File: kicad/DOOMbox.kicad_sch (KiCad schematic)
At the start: 13 parts, among them J1 DE15_Socket_HighDensity, U1 RPi Pico 2, U2 MCP23S08

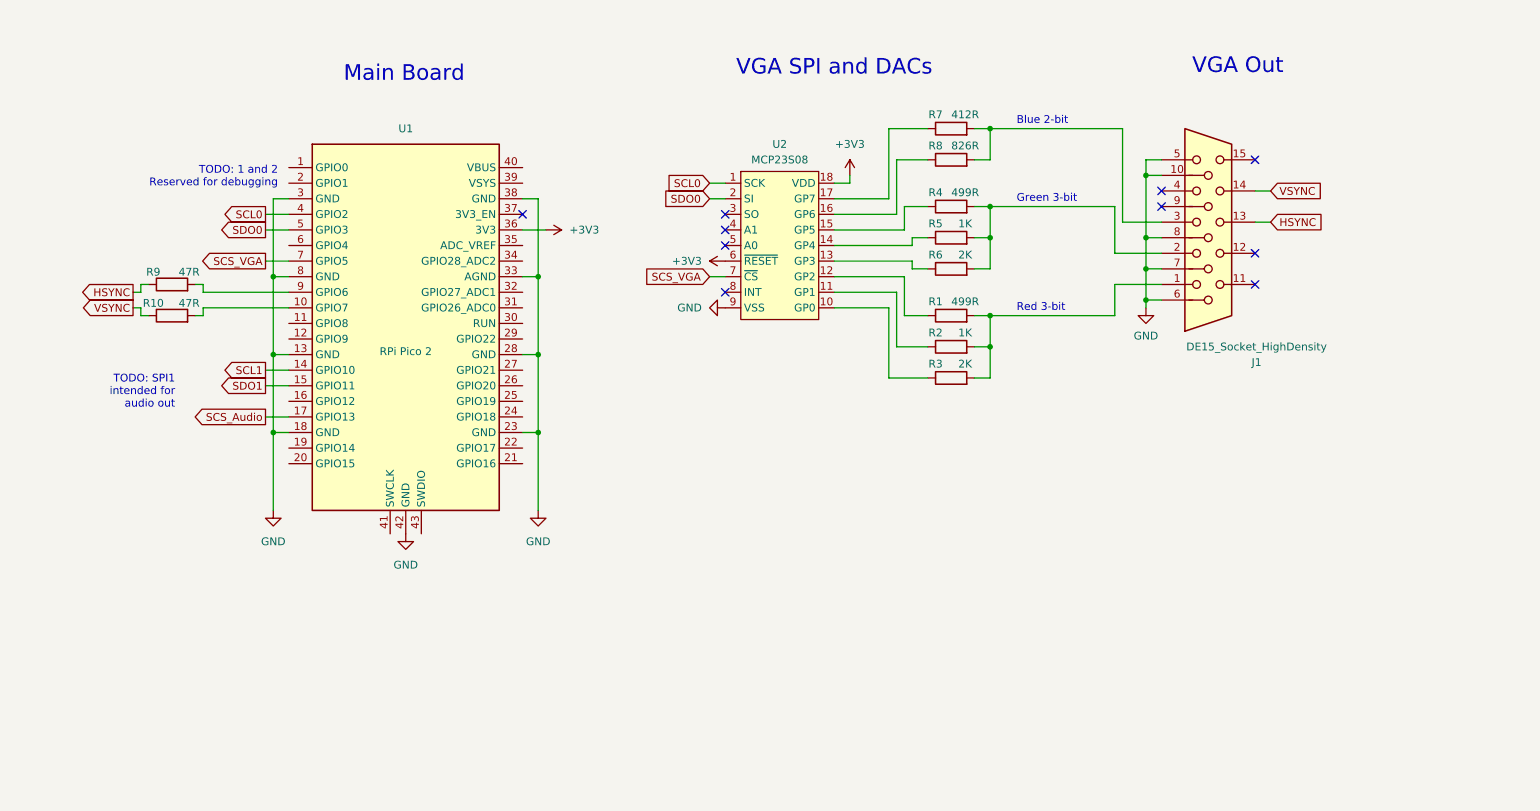
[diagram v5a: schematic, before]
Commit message: Document inputs and storage info, and add PWM audio schematic
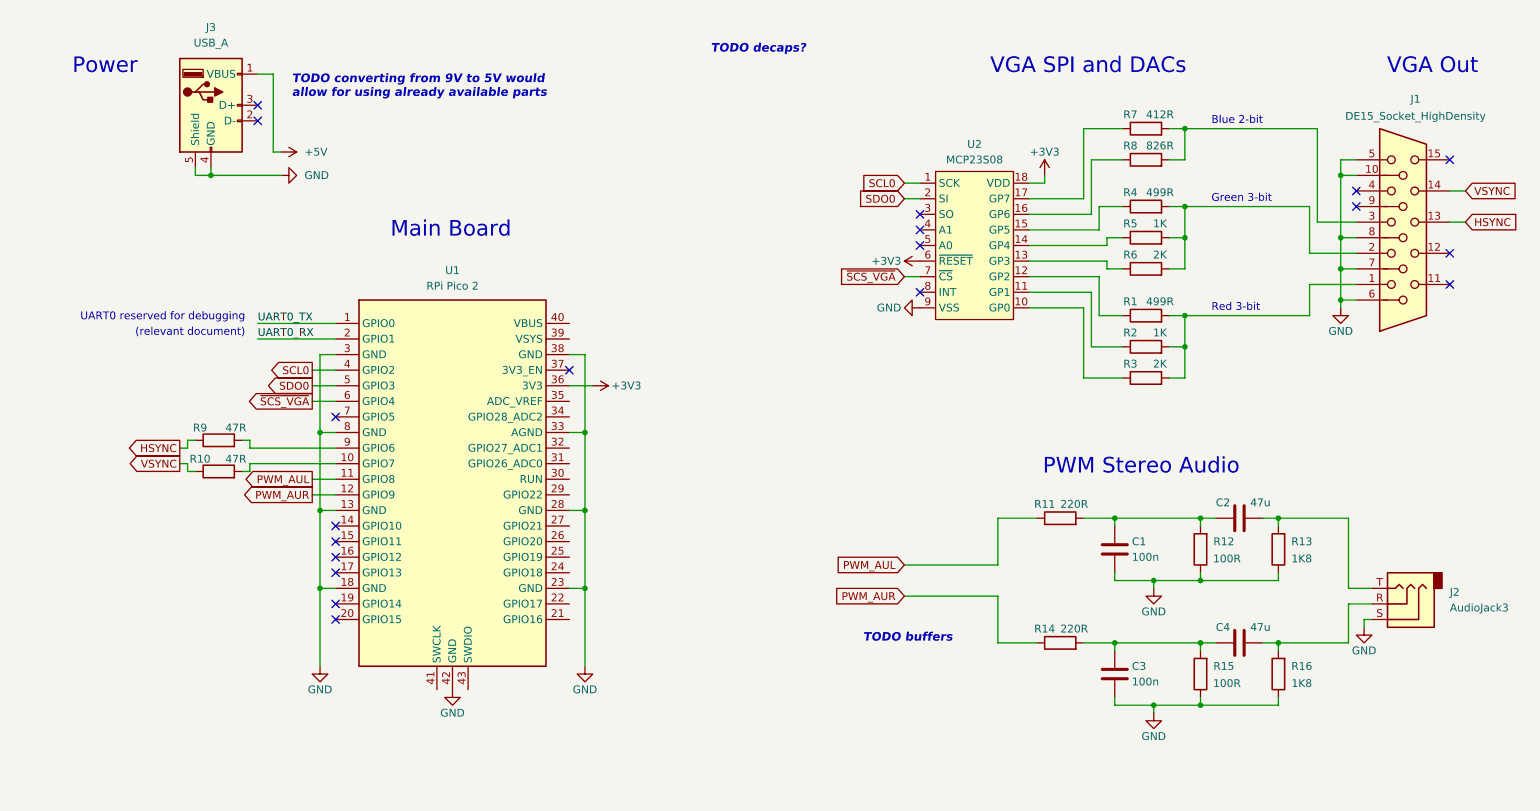
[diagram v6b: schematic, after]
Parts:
- added C1, C3: 100n, symbol Device:C
- added C2, C4: 47u, symbol Device:C
- added J2: AudioJack3, symbol Connector_Audio:AudioJack3
- added J3: USB_A, symbol Connector:USB_A
- added R11, R14: 220R, symbol Device:R
- added R12, R15: 100R, symbol Device:R
- added R13, R16: 1K8, symbol Device:R
- U1: symbol MCU_RPi:RPi_Pico_SMD_TH -> Doombox:RPi_Pico_SMD_TH
- U2: symbol MCU_Microchip_MCP:MCP23S08 -> Doombox:MCP23S08
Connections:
- net GND: now also C1.2, C3.2, J2.S, J3.4 (GND), J3.5 (Shield), R12.1, R13.1, R15.1, R16.1
- net UART0_TX: now reaches U1.1 (GPIO0)
- net PWM_AUL: now reaches U1.11 (GPIO8)
- net PWM_AUL: now also R11.1
- net PWM_AUR: now reaches U1.12 (GPIO9)
- net PWM_AUR: now also R14.1
- net UART0_RX: now reaches U1.2 (GPIO1)
- net ~{SCS_VGA}: now reaches U1.6 (GPIO4)
- net ~{SCS_VGA}: now also U2.7 (~{CS})
- net SCL1: no longer names the net of U1.14 (GPIO10)
- net SCS_Audio: no longer names the net of U1.17 (GPIO13)
- net SCS_VGA: no longer names the net of U1.7 (GPIO5)
- net SCS_VGA: no longer U2.7 (~{CS})
- net SDO1: no longer names the net of U1.15 (GPIO11)
- new net: C2.2, J2.T, R13.2
- new net: C3.1, C4.1, R14.2, R15.2
- new net: C1.1, C2.1, R11.2, R12.2
- new net: C4.2, J2.R, R16.2
- new net +5V: J3.1 (VBUS)
- no-connect marks 10 -> 19
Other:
- note added: "(relevant document)"
- note added: "PWM Stereo Audio"
- note added: "Power"
- note added: "TODO buffers"
- note added: "TODO converting from 9V to 5V would allow for using already available parts"
- note added: "TODO decaps?"
- note added: "UART0 reserved for debugging"
- note removed: "TODO: 1 and 2 Reserved for debugging"
- note removed: "TODO: SPI1 intended for audio out"
- company: (none) -> Jack Bennett
- title: (none) -> The DOOMbox
- moved on the sheet: J1, R1, R10, R2, R3, R4, R5, R6, R7, R8, R9, U1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

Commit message: Schem for power circuit + rpi SWD pins and reset button
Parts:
- removed J3: USB_A, symbol Connector:USB_A
- added C5: 1u, symbol Device:C
- added C6: 2u2, symbol Device:C
- added D1: D, symbol Device:D
- added D2: LED, symbol Device:LED
- added R17: 220R, symbol Device:R
- added SW1: SW_SPST, symbol Switch:SW_SPST
- added SW2: SW_Push, symbol Switch:SW_Push
- added U3: AP7381-50SA-7, Package_TO_SOT_SMD:SOT-23, symbol Regulator_Linear:AP7381-50SA-7
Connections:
- net +5V: now also C6.1, D1.2 (A), D2.1 (K), R17.1, U3.2 (VO)
- net GND: now also C5.2, C6.2, SW2.2, U3.3 (GND)
- net at U1.30 (RUN): now also SW2.1
- net at U1.39 (VSYS): now also D1.1 (K)
- net SWCLK: now reaches U1.41 (SWCLK)
- net SWDIO: now reaches U1.43 (SWDIO)
- new net: C5.1, SW1.2 (B), U3.1 (VI)
- new net: D2.2 (A), R17.2
- new net VDC: SW1.1 (A)
- no-connect marks 19 -> 11
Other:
- note added: "To order (not yet doc'd): - necessary resistors - necessary caps - diodes? (if schottky needed) - phone connector (J2)"
- note added: "UART0 reserved for debugging (so is SWD, also for programming)"
- note added: "power LED worth ~20mA?"
- note removed: "(relevant document)"
- note removed: "TODO converting from 9V to 5V would allow for using already available parts"
- note removed: "UART0 reserved for debugging"
- moved on the sheet: R10, R9, U1

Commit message: Clean up symbols and add footprint for MCP23S08
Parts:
- U1: symbol Doombox:RPi_Pico_SMD_TH -> MCU_RPi:RPi_Pico_SMD_TH
- U2: symbol Doombox:MCP23S08 -> MCU_Microchip_MCP:MCP23S08
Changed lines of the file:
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@@
 	)
 	(symbol
-		(lib_id "Doombox:MCP23S08")
+		(lib_id "MCU_Microchip_MCP:MCP23S08")
 		(at 171.45 53.34 0)
 		(unit 1)
@@
 	)
 	(symbol
-		(lib_id "Doombox:RPi_Pico_SMD_TH")
+		(lib_id "MCU_RPi:RPi_Pico_SMD_TH")
 		(at 90.17 92.71 0)
 		(unit 1)
